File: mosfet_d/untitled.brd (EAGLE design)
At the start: 60.9 x 44.1 mm, 47 parts

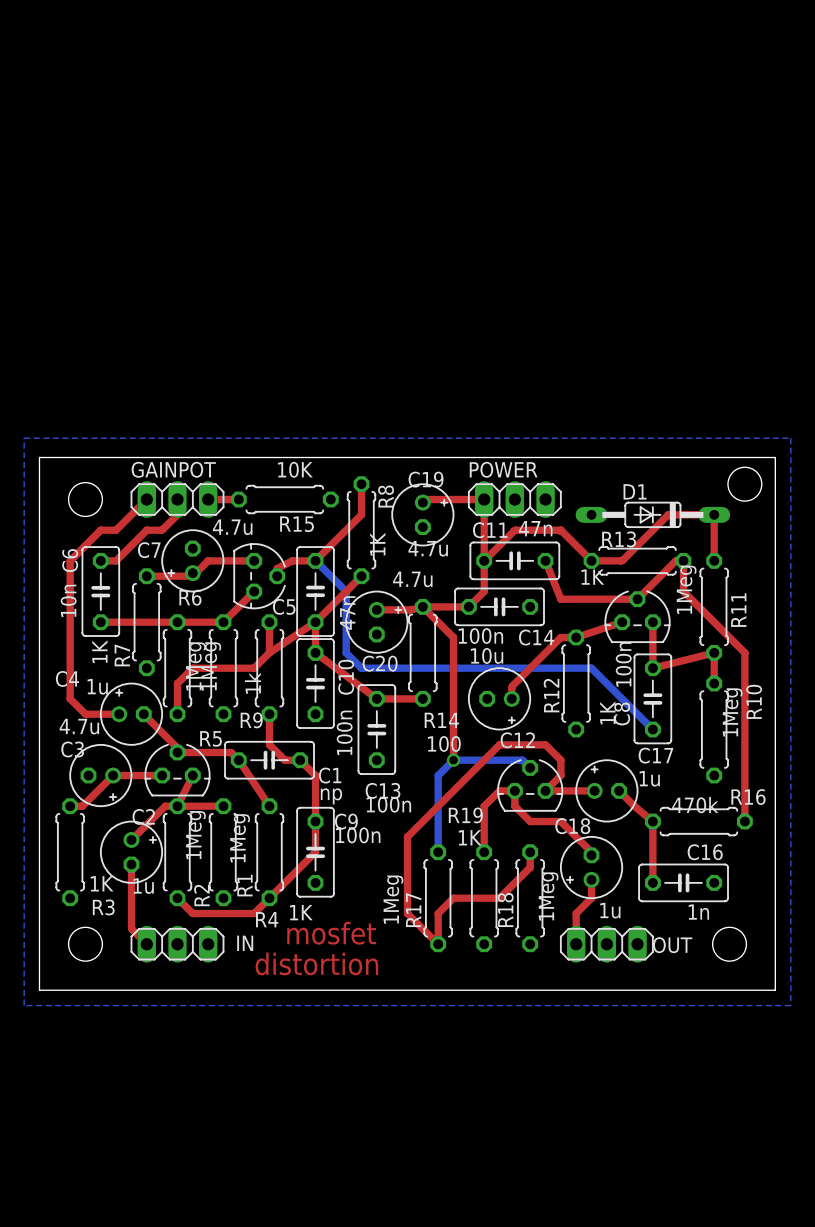
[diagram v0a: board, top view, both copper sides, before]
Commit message: fixed pinout of transistors in mosfet d
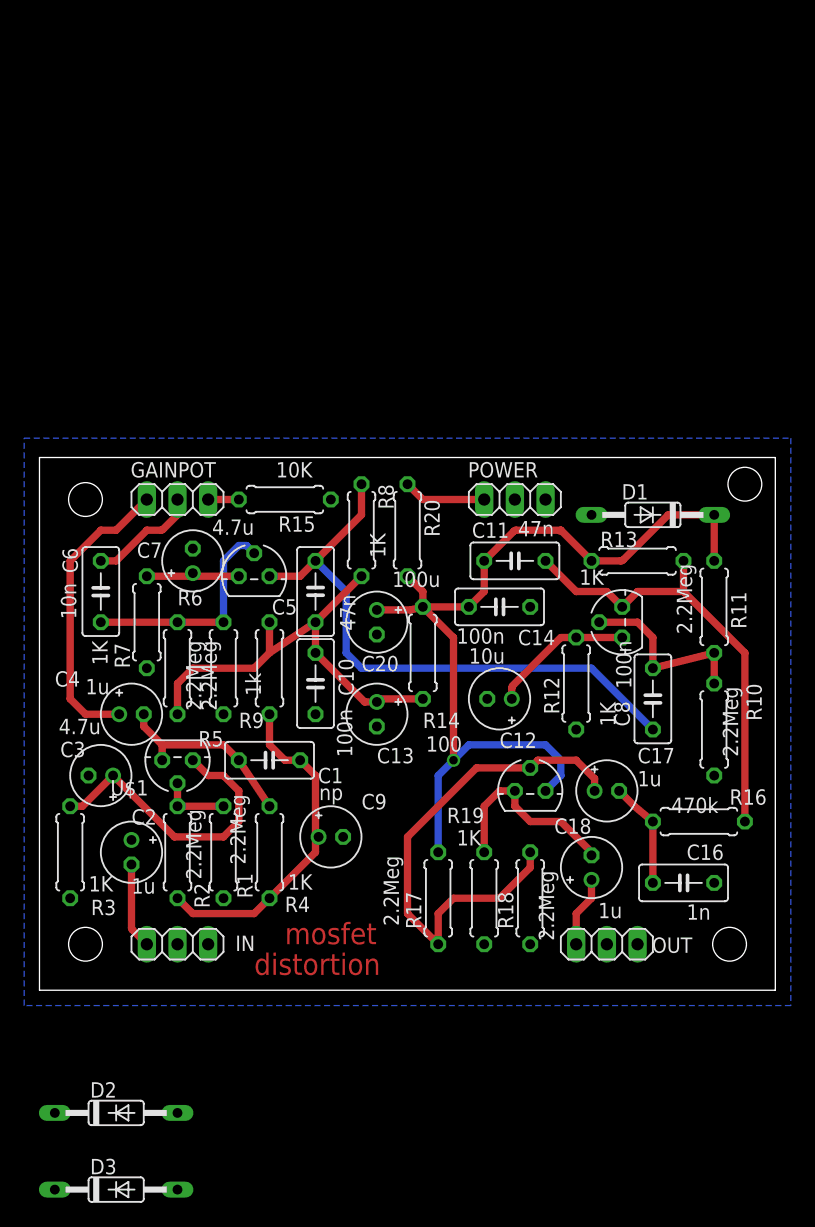
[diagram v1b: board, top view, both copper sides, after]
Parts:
- removed C19: 4.7u, dan:E2-5
- added D2, D3: 1N4148DO35-10, dan:DO35-10
- added R20: 100, dan:0207/7
- C13, C9: value 100n -> 4.7u; device dan:C050-030X075 -> dan:E2-5
- C20: value 4.7u -> 100u
- R1, R10, R11, R17, R18, R2, R5, R6: value 1Meg -> 2.2Meg
- moved C9 1.80 mm to (24.1, 12.7), turned to 0 degrees
- moved U$3 1.27 mm to (48.3, 30.5), turned to 90 degrees
- moved C13 1.27 mm to (27.9, 22.9)
- moved U$1 1.27 mm to (11.4, 19.1), turned to 180 degrees
- turned U$2 to 0 degrees
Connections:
- new net N$17: C2.+
- new net N$18: POWER.1, R20.1
- net GND: now also C13.-, C9.-, D2.A; no longer C13.2, C19.-, C9.2
- net N$1: now also D2.C, D3.A, U$1.2; no longer C2.+, U$1.3
- net N$12: now also U$3.3; no longer U$3.2
- net N$13: now also C13.+; no longer C13.1
- net N$15: now also U$3.2; no longer U$3.3
- net N$19: now also U$4.2; no longer U$4.3
- net N$2: now also U$1.3; no longer U$1.2
- net N$20: now also R20.2, U$4.3; no longer C19.+, POWER.1, U$4.2
- net N$3: now also C9.+, D3.C; no longer C9.1
- net N$6: now also U$2.2; no longer U$2.3
- net N$7: now also U$2.3; no longer U$2.2
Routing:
- net N$5: track 8.67 -> 25.1 mm
- net N$18: track 0.00 -> 6.88 mm
- net N$1: track 11.6 -> 5.71 mm
- net N$6: track 13.8 -> 18.6 mm
- net N$19: track 46.5 -> 42.7 mm
- net N$15: track 11.6 -> 15.3 mm
- net N$9: track 9.67 -> 7.87 mm
- net N$2: track 14.3 -> 15.9 mm
- net N$12: track 38.6 -> 37.2 mm
- net N$20: track 77.4 -> 76.6 mm
- net N$13: track 36.4 -> 36.9 mm

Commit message: fixed component values in mosfet d
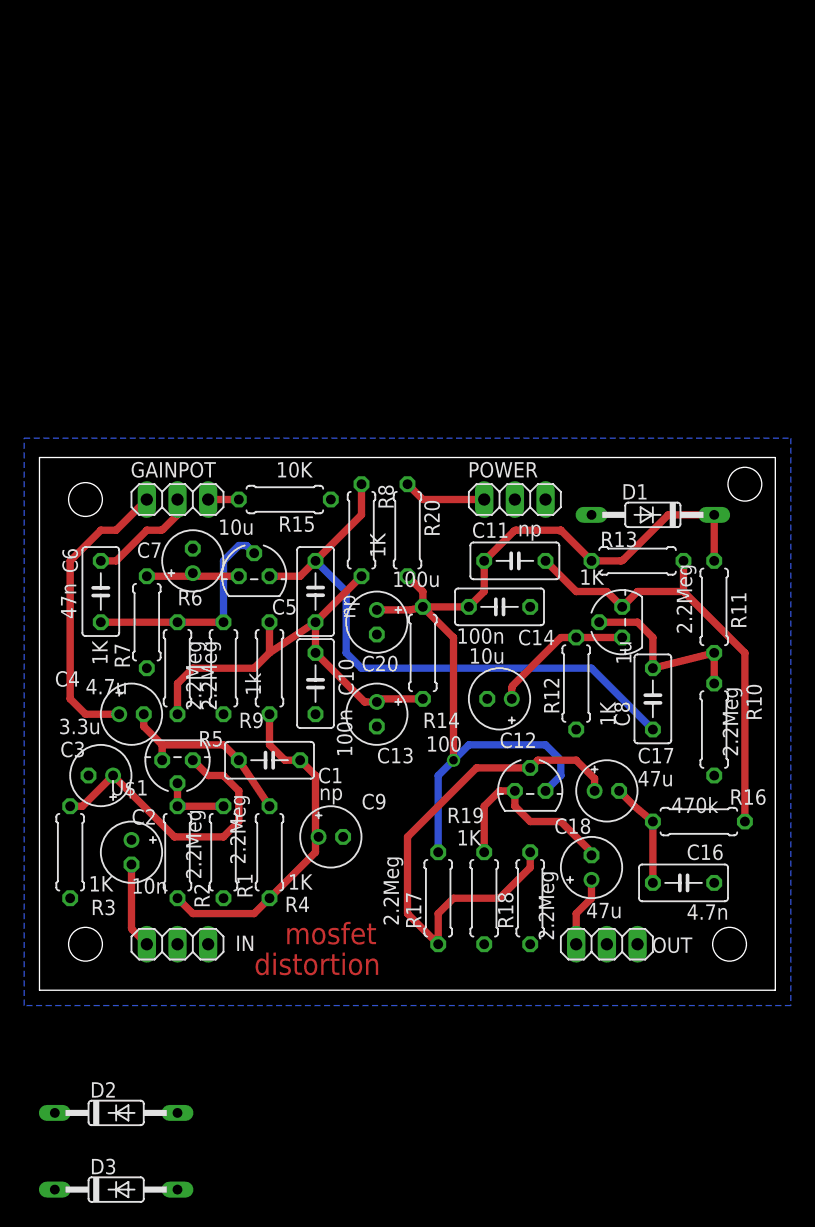
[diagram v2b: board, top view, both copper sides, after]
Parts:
- C11, C5: value 47n -> np
- C16: value 1n -> 4.7n
- C17, C18: value 1u -> 47u
- C2: value 1u -> 10n
- C3: value 4.7u -> 3.3u
- C4: value 1u -> 4.7u
- C6: value 10n -> 47n
- C7: value 4.7u -> 10u
- C8: value 100n -> 1u
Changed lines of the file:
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@@
 <attribute name="VALUE" x="25.908" y="19.304" size="1.27" layer="21" font="vector" ratio="15" rot="R90"/>
 </element>
-<element name="C11" library="dan" package="C050-030X075" value="47n" x="39.37" y="35.56" smashed="yes">
+<element name="C11" library="dan" package="C050-030X075" value="np" x="39.37" y="35.56" smashed="yes">
 <attribute name="NAME" x="35.814" y="37.465" size="1.27" layer="21" font="vector" ratio="15"/>
 <attribute name="VALUE" x="39.624" y="37.592" size="1.27" layer="21" font="vector" ratio="15"/>
@@
 <attribute name="VALUE" x="34.544" y="28.702" size="1.27" layer="21" font="vector" ratio="15"/>
 </element>
-<element name="C16" library="dan" package="C050-030X075" value="1n" x="53.34" y="8.89" smashed="yes">
+<element name="C16" library="dan" package="C050-030X075" value="4.7n" x="53.34" y="8.89" smashed="yes">
 <attribute name="NAME" x="53.594" y="10.795" size="1.27" layer="21" font="vector" ratio="15"/>
 <attribute name="VALUE" x="53.594" y="5.842" size="1.27" layer="21" font="vector" ratio="15"/>
 </element>
-<element name="C17" library="dan" package="E2-5" value="1u" x="46.99" y="16.51" smashed="yes">
+<element name="C17" library="dan" package="E2-5" value="47u" x="46.99" y="16.51" smashed="yes">
 <attribute name="NAME" x="49.53" y="18.796" size="1.27" layer="21" font="vector" ratio="15"/>
 <attribute name="VALUE" x="49.53" y="16.891" size="1.27" layer="21" font="vector" ratio="15"/>
 </element>
-<element name="C18" library="dan" package="E2-5" value="1u" x="45.72" y="10.16" smashed="yes" rot="R90">
+<element name="C18" library="dan" package="E2-5" value="47u" x="45.72" y="10.16" smashed="yes" rot="R90">
 <attribute name="NAME" x="45.72" y="14.224" size="1.27" layer="21" font="vector" ratio="15" rot="R180"/>
 <attribute name="VALUE" x="48.26" y="7.239" size="1.27" layer="21" font="vector" ratio="15" rot="R180"/>
 </element>
-<element name="C2" library="dan" package="E2-5" value="1u" x="7.62" y="11.43" smashed="yes" rot="R270">
+<element name="C2" library="dan" package="E2-5" value="10n" x="7.62" y="11.43" smashed="yes" rot="R270">
 <attribute name="NAME" x="7.62" y="13.716" size="1.27" layer="21" font="vector" ratio="15"/>
 <attribute name="VALUE" x="7.62" y="8.001" size="1.27" layer="21" font="vector" ratio="15"/>
@@
 <attribute name="VALUE" x="29.21" y="33.401" size="1.27" layer="21" font="vector" ratio="15"/>
 </element>
-<element name="C3" library="dan" package="E2-5" value="4.7u" x="5.08" y="17.78" smashed="yes" rot="R180">
+<element name="C3" library="dan" package="E2-5" value="3.3u" x="5.08" y="17.78" smashed="yes" rot="R180">
 <attribute name="NAME" x="3.81" y="20.574" size="1.27" layer="21" font="vector" ratio="15" rot="R180"/>
 <attribute name="VALUE" x="5.08" y="22.479" size="1.27" layer="21" font="vector" ratio="15" rot="R180"/>
 </element>
-<element name="C4" library="dan" package="E2-5" value="1u" x="7.62" y="22.86" smashed="yes">
+<element name="C4" library="dan" package="E2-5" value="4.7u" x="7.62" y="22.86" smashed="yes">
 <attribute name="NAME" x="1.27" y="25.146" size="1.27" layer="21" font="vector" ratio="15"/>
 <attribute name="VALUE" x="3.81" y="24.511" size="1.27" layer="21" font="vector" ratio="15"/>
 </element>
-<element name="C5" library="dan" package="C050-030X075" value="47n" x="22.86" y="33.02" smashed="yes" rot="R90">
+<element name="C5" library="dan" package="C050-030X075" value="np" x="22.86" y="33.02" smashed="yes" rot="R90">
 <attribute name="NAME" x="21.336" y="32.385" size="1.27" layer="21" font="vector" ratio="15" rot="R180"/>
 <attribute name="VALUE" x="24.892" y="32.766" size="1.27" layer="21" font="vector" ratio="15" rot="R270"/>
 </element>
-<element name="C6" library="dan" package="C050-030X075" value="10n" x="5.08" y="33.02" smashed="yes" rot="R270">
+<element name="C6" library="dan" package="C050-030X075" value="47n" x="5.08" y="33.02" smashed="yes" rot="R270">
 <attribute name="NAME" x="3.175" y="34.544" size="1.27" layer="21" font="vector" ratio="15" rot="R90"/>
 <attribute name="VALUE" x="3.048" y="30.734" size="1.27" layer="21" font="vector" ratio="15" rot="R90"/>
 </element>
-<element name="C7" library="dan" package="E2-5" value="4.7u" x="12.7" y="35.56" smashed="yes" rot="R90">
+<element name="C7" library="dan" package="E2-5" value="10u" x="12.7" y="35.56" smashed="yes" rot="R90">
 <attribute name="NAME" x="10.16" y="37.084" size="1.27" layer="21" font="vector" ratio="15" rot="R180"/>
 <attribute name="VALUE" x="17.78" y="38.989" size="1.27" layer="21" font="vector" ratio="15" rot="R180"/>
 </element>
-<element name="C8" library="dan" package="C050-030X075" value="100n" x="50.8" y="24.13" smashed="yes" rot="R270">
+<element name="C8" library="dan" package="C050-030X075" value="1u" x="50.8" y="24.13" smashed="yes" rot="R270">
 <attribute name="NAME" x="48.895" y="21.844" size="1.27" layer="21" font="vector" ratio="15" rot="R90"/>
 <attribute name="VALUE" x="47.752" y="28.956" size="1.27" layer="21" font="vector" ratio="15" rot="R270"/>

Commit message: added pcb mounted pots to distortion
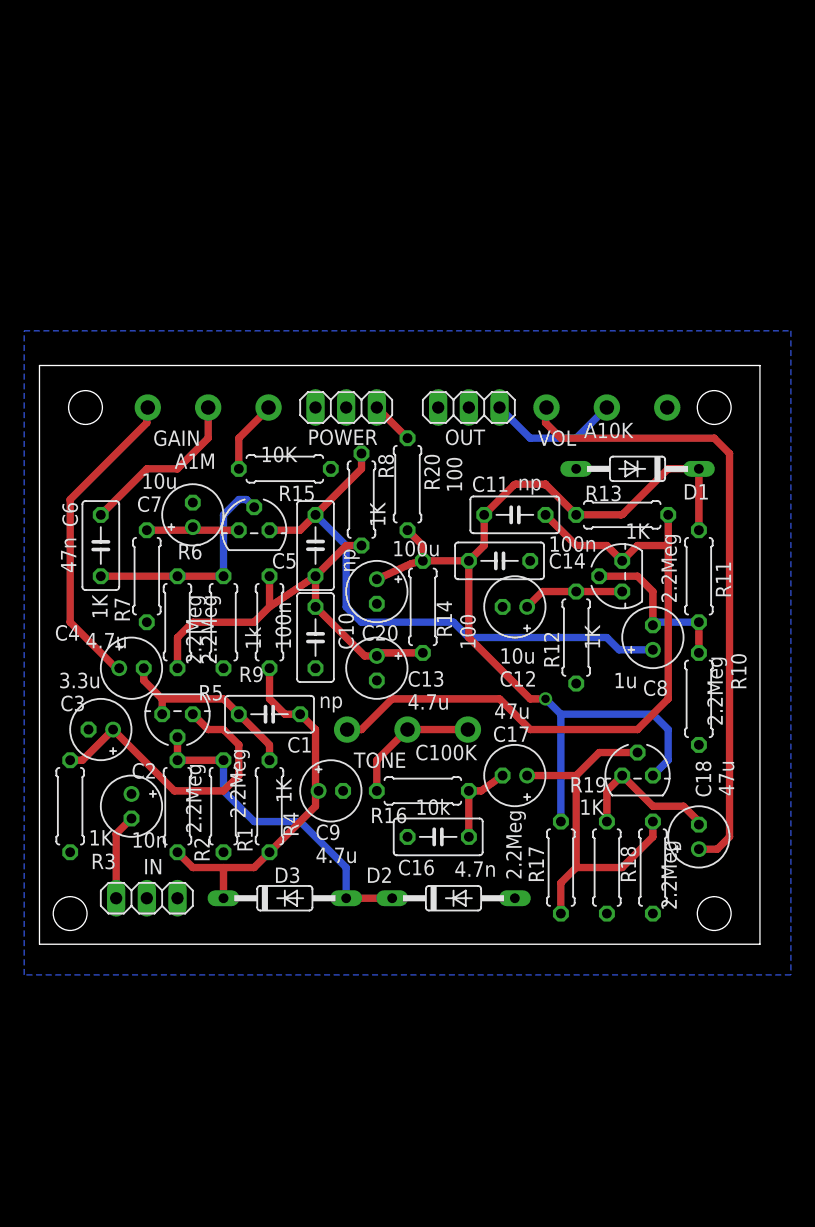
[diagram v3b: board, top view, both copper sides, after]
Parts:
- removed GAINPOT: (no value), dan:1X03
- added GAIN: A1M, dan:3RP/1610N
- added TONE: C100K, dan:3RP/1610N
- added VOL: A10K, dan:3RP/1610N
- C8: device dan:C050-030X075 -> dan:E2-5
- R16: value 470k -> 10k
- moved OUT 45.9 mm to (35.6, 48.3), turned to 180 degrees
- moved D2 33.1 mm to (34.3, 7.62)
- moved D3 27.9 mm to (20.3, 7.62)
- moved R16 23.0 mm to (31.8, 16.5), turned to 180 degrees
- moved C16 20.7 mm to (33.0, 12.7), turned to 180 degrees
- moved POWER 15.9 mm to (25.4, 48.3), turned to 180 degrees
- moved R19 10.5 mm to (47.0, 10.2)
- moved R17 10.5 mm to (43.2, 10.2)
- moved R18 10.5 mm to (50.8, 10.2)
- moved C18 9.25 mm to (54.6, 12.7)
- moved U$4 8.98 mm to (49.5, 17.8)
- moved C17 7.73 mm to (39.4, 17.8), turned to 180 degrees
- moved C12 7.73 mm to (39.4, 31.8)
- moved C8 5.08 mm to (50.8, 29.2), turned to 90 degrees
- moved IN 4.58 mm to (8.89, 7.62)
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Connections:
- new net N$21: R16.2, TONE.2, TONE.3
- new net N$25: OUT.1, VOL.2
- net GND: now also VOL.3
- net N$11: now also GAIN.2; no longer GAINPOT.2
- net N$12: now also TONE.1; no longer R16.2
- net N$15: now also C8.-; no longer C8.1
- net N$16: now also GAIN.3; no longer GAINPOT.3
- net N$23: now also VOL.1; no longer OUT.1
- net N$4: now also GAIN.1; no longer GAINPOT.1
- net N$7: now also C8.+; no longer C8.2
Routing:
- net N$23: track 5.86 -> 52.3 mm
- net N$1: track 5.71 -> 27.4 mm
- net N$12: track 37.2 -> 57.3 mm
- net N$19: track 42.7 -> 30.6 mm
- net N$21: track 0.00 -> 11.1 mm
- net N$25: track 0.00 -> 11.0 mm
- net N$11: track 9.18 -> 14.1 mm
- net N$20: track 76.6 -> 81.2 mm
- net N$22: track 16.3 -> 12.5 mm
- net N$16: track 2.54 -> 6.10 mm
- net N$14: track 11.8 -> 8.40 mm
- net N$18: track 6.88 -> 3.59 mm
- net N$3: track 28.0 -> 30.6 mm
- net N$7: track 49.0 -> 46.5 mm
- net N$10: track 8.86 -> 7.01 mm
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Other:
- board size 60.9 x 44.1 mm -> 59.7 x 47.9 mm
- board text removed: "distortion"
- board text removed: "mosfet"

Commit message: redesigned the distortion pcb
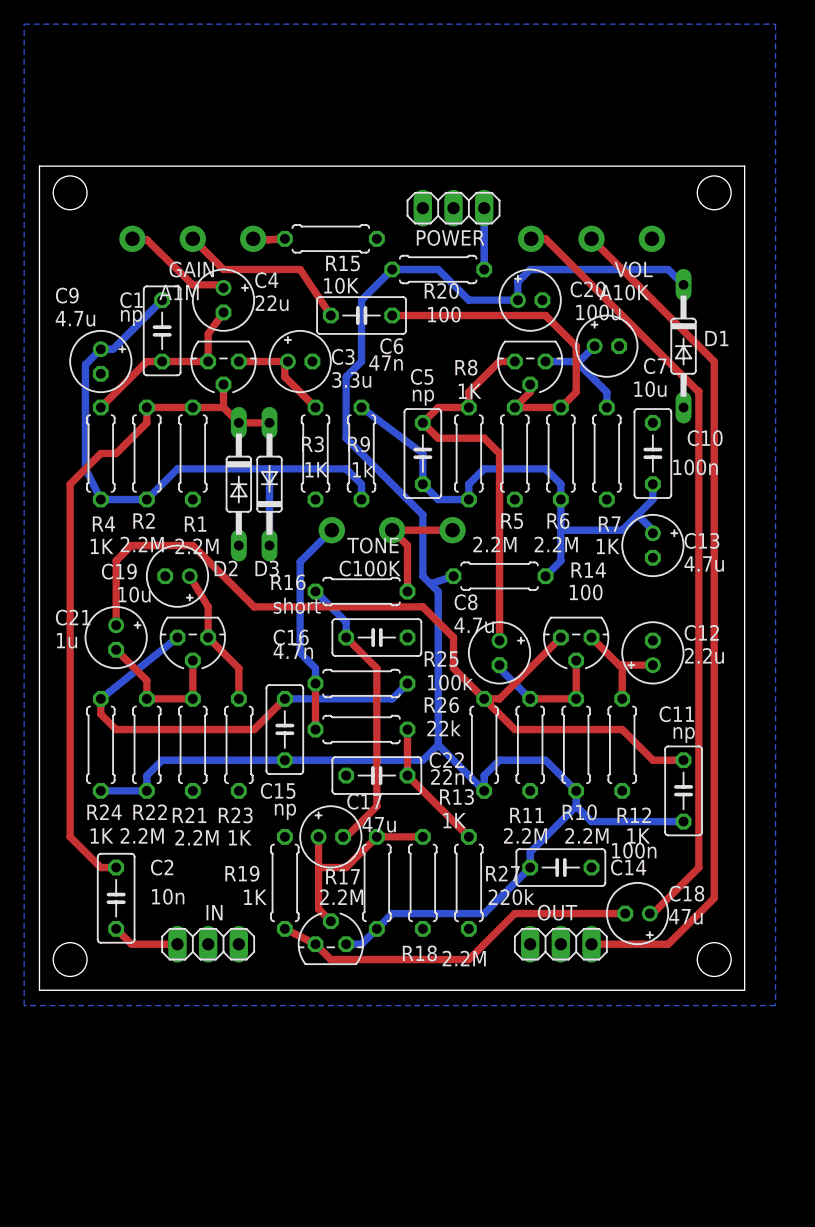
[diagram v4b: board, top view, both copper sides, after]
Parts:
- added C15: np, dan:C050-030X075
- added C19: 10u, dan:E2-5
- added C21: 1u, dan:E2-5
- added C22: 22n, dan:C050-030X075
- added R21, R22: 2.2M, dan:0207/7
- added R23, R24: 1K, dan:0207/7
- added R25: 100k, dan:0207/7
- added R26: 22k, dan:0207/7
- added R27: 220k, dan:0207/7
- added U$5: 2N7000_2, dan:TO92
- C12: value 10u -> 2.2u
- C2: device dan:E2-5 -> dan:C050-030X075
- C4: value 4.7u -> 22u
- C8: value 1u -> 4.7u
- R1, R10, R11, R17, R18, R2, R5, R6: value 2.2Meg -> 2.2M
- R16: value 10k -> short
- moved OUT 45.1 mm to (43.2, 3.81)
- moved C9 40.3 mm to (5.08, 52.1), turned to 270 degrees
- moved R7 39.4 mm to (47.0, 44.5)
- moved D2 38.6 mm to (16.5, 41.9), turned to 270 degrees
- moved C7 37.0 mm to (47.0, 53.3), turned to 0 degrees
- moved R3 35.6 mm to (22.9, 44.5)
- moved R6 34.7 mm to (43.2, 44.5)
- moved C3 34.7 mm to (21.6, 52.1), turned to 0 degrees
- moved D3 34.3 mm to (19.1, 41.9), turned to 90 degrees
- moved C1 33.0 mm to (10.2, 54.6), turned to 270 degrees
- moved R4 32.4 mm to (5.08, 44.5)
- moved C10 31.8 mm to (50.8, 44.5), turned to 90 degrees
- moved C4 31.4 mm to (15.2, 57.1), turned to 270 degrees
- moved U$1 29.5 mm to (15.2, 52.1)
- moved R1 29.3 mm to (12.7, 44.5)
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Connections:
- removed net N$17: C2.+
- new net N$24: C15.2, R24.1, R25.2, U$5.3
- new net N$26: C19.+, R23.2, U$5.1
- new net N$27: C21.-, R21.2, R22.1, U$5.2
- new net N$28: C22.1, R26.2, R27.1
- new net N$29: R25.1, R26.1, TONE.1
- net GND: now also C19.-, C22.2, R21.1, R23.1, R27.2
- net N$1: now also C2.1
- net N$12: now also C21.+; no longer TONE.1
- net N$20: now also C15.1, R22.2, R24.2
- net N$8: now also C2.2; no longer C2.-
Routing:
- net N$20: track 81.2 -> 155.1 mm, vias 1 -> 0
- net N$25: track 11.0 -> 70.6 mm
- net N$24: track 0.00 -> 36.9 mm
- net N$1: track 27.4 -> 56.4 mm
- net N$3: track 30.6 -> 50.8 mm
- net N$29: track 0.00 -> 18.1 mm
- net N$22: track 12.5 -> 30.6 mm
- net N$4: track 26.1 -> 9.32 mm
- net N$10: track 7.01 -> 23.7 mm
- net N$5: track 25.1 -> 9.29 mm
- net N$7: track 46.5 -> 33.4 mm
- net N$12: track 57.3 -> 70.2 mm
- net N$19: track 30.6 -> 17.7 mm
- net N$27: track 0.00 -> 12.1 mm
- net N$23: track 52.3 -> 64.2 mm
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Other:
- board size 59.7 x 47.9 mm -> 58.4 x 68.2 mm
